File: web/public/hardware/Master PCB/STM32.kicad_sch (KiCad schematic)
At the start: 28 parts, among them SW1 nRST, U1 STM32U585VITx, U5 MAX7375AXR805

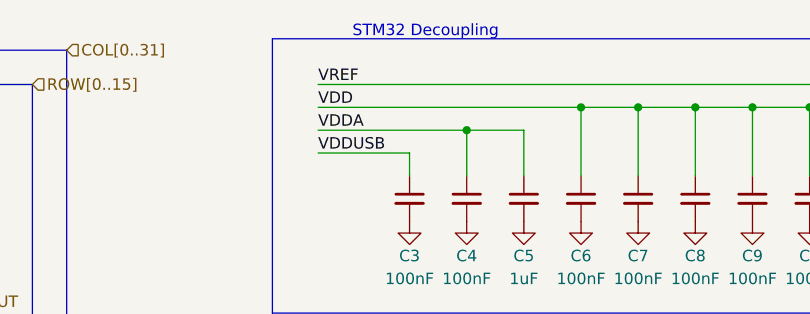
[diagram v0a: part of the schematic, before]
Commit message: Fix encoder schematic and miscellaneous cleanup (new date, etc.)
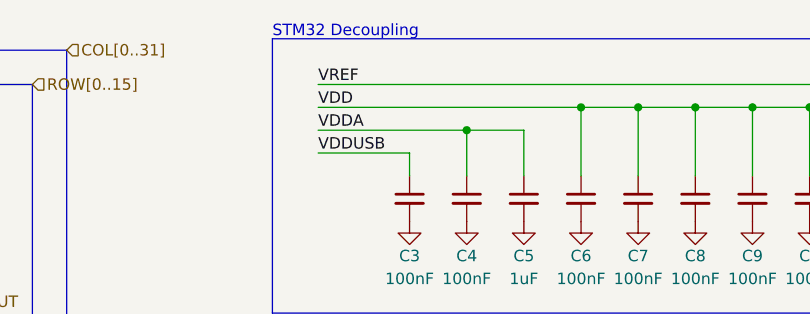
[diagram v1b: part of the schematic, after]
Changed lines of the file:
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@@
     (effects (font (size 1.27 1.27)) (justify left bottom))
   )
-  (text "STM32 Decoupling" (at 186.69 17.78 0)
+  (text "STM32 Decoupling" (at 177.8 17.78 0)
     (effects (font (size 1.27 1.27)) (justify left bottom))
   )

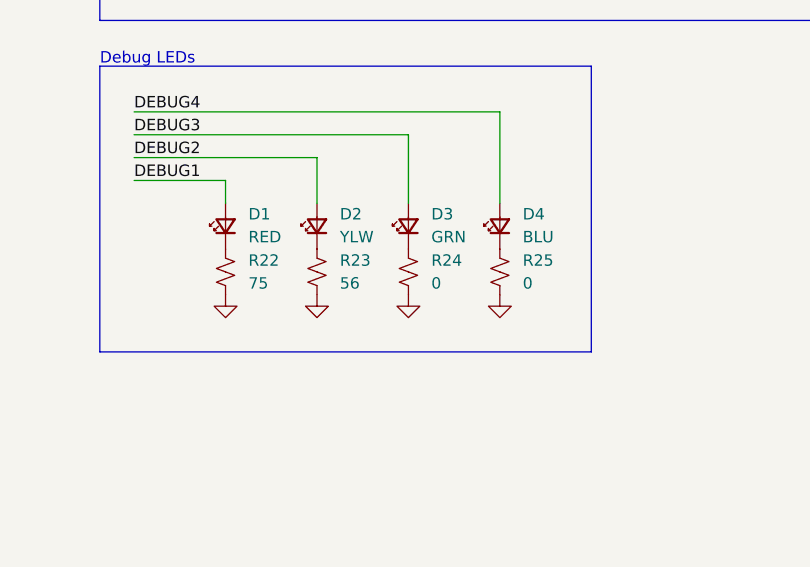
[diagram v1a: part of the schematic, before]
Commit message: Change LED resistor values
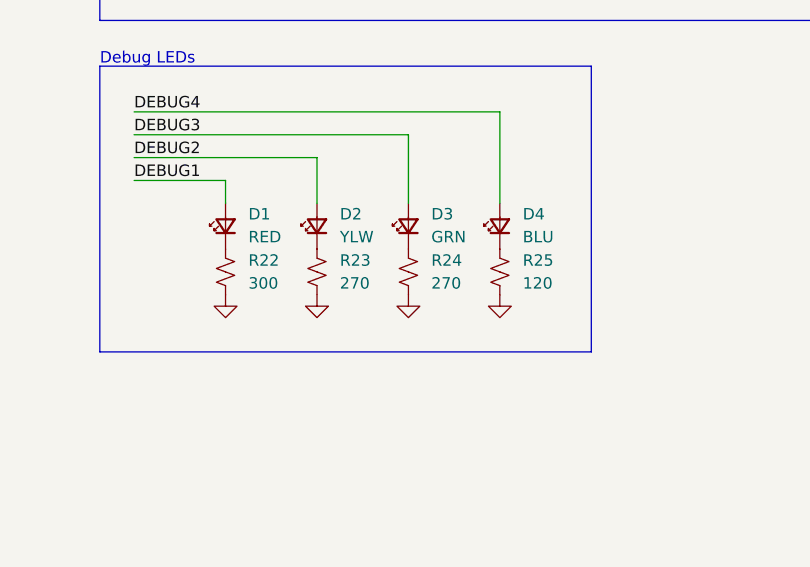
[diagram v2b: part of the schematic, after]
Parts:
- R22: value 75 -> 300
- R23: value 56 -> 270
- R24: value 0 -> 270
- R25: value 0 -> 120
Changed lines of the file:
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@@
       (effects (font (size 1.27 1.27)) (justify left))
     )
-    (property "Value" "0" (at 214.63 77.47 0)
+    (property "Value" "270" (at 214.63 77.47 0)
       (effects (font (size 1.27 1.27)) (justify left))
     )
@@
       (effects (font (size 1.27 1.27)) (justify left))
     )
-    (property "Value" "0" (at 224.79 77.47 0)
+    (property "Value" "120" (at 224.79 77.47 0)
       (effects (font (size 1.27 1.27)) (justify left))
     )
@@
       (effects (font (size 1.27 1.27)) (justify left))
     )
-    (property "Value" "75" (at 194.31 77.47 0)
+    (property "Value" "300" (at 194.31 77.47 0)
       (effects (font (size 1.27 1.27)) (justify left))
     )
@@
       (effects (font (size 1.27 1.27)) (justify left))
     )
-    (property "Value" "56" (at 204.47 77.47 0)
-      (effects (font (size 1.27 1.27)) (justify left))
-    )
+    (property "Value" "270" (at 204.47 77.47 0)
+      (effects (font (size 1.27 1.27)) (justify left))
+    )
